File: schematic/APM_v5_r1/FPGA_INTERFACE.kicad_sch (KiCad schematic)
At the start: 6 parts, among them J1 DF40C-60DS-0.4V(51), J15 FPGA FFC, J21 FPGA FMC, J3 DF40C-60DS-0.4V(51)

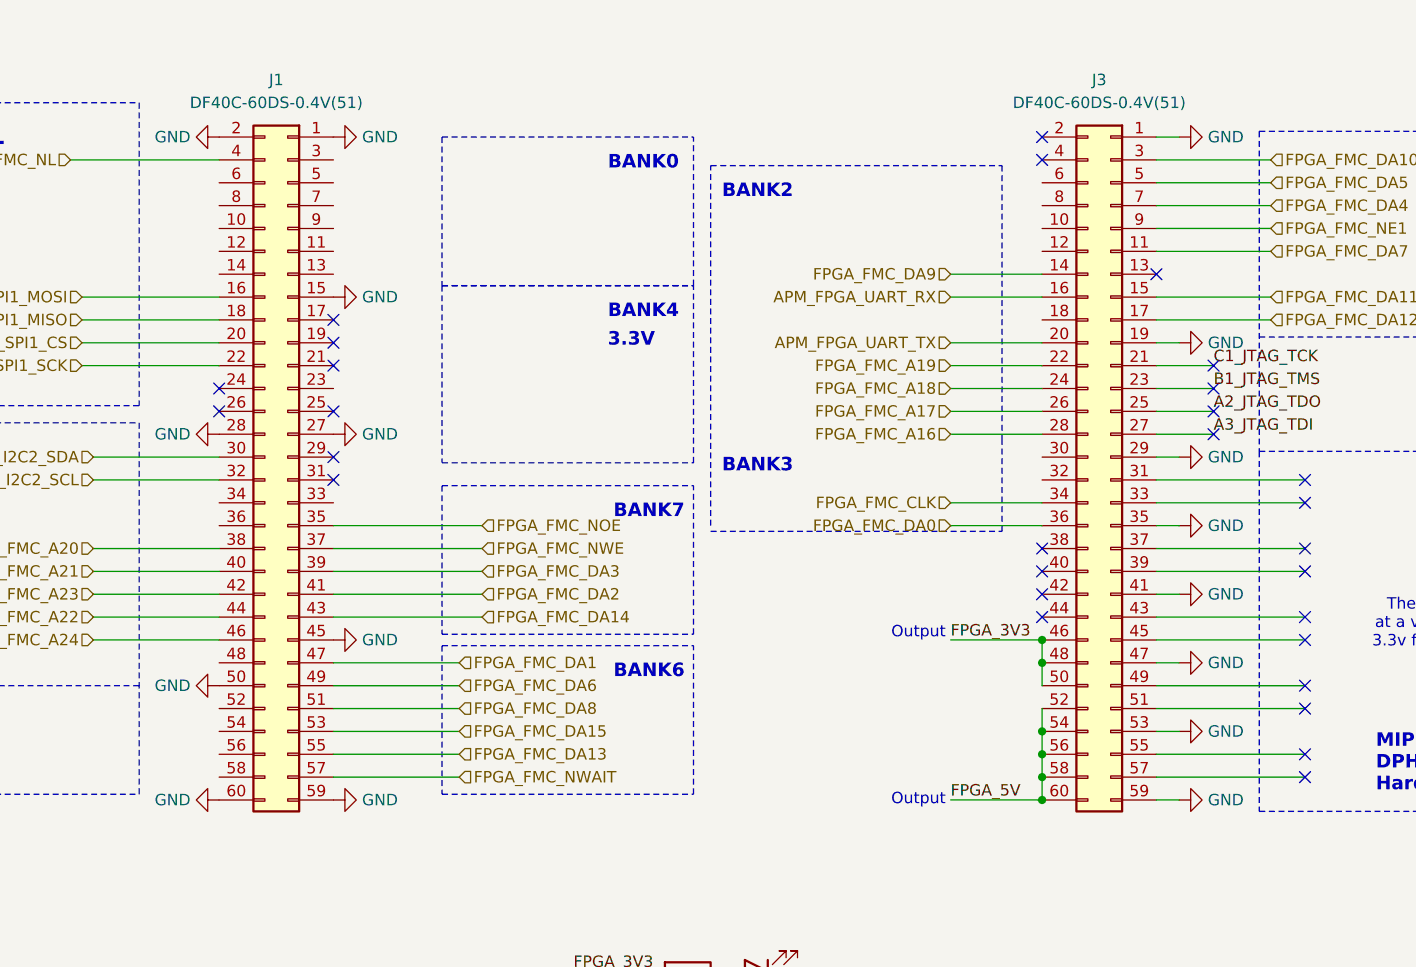
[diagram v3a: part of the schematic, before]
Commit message: schematic for the oscillator board
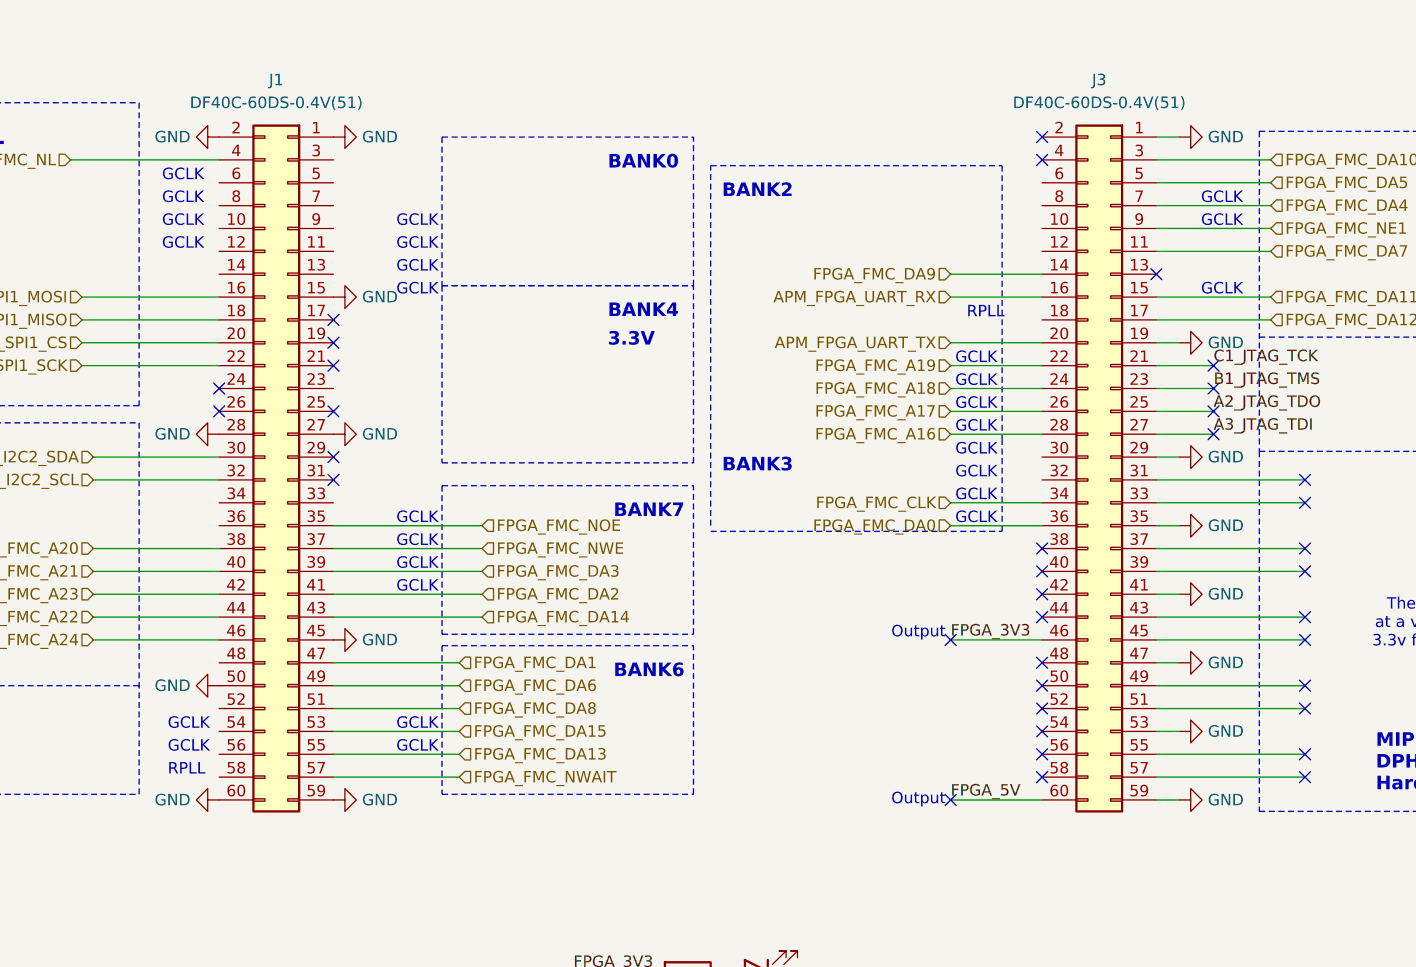
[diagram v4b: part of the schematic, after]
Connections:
- net FPGA_3V3: no longer J3.48 (Pin_48), J3.50 (Pin_50)
- net FPGA_5V: no longer J3.52 (Pin_52), J3.54 (Pin_54), J3.56 (Pin_56), J3.58 (Pin_58)
- no-connect marks 40 -> 48
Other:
- note added: "GCLK"
- note added: "RPLL"
